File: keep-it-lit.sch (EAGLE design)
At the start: 33 parts, among them IC1 74AHCT1G04DBV, Q1 BSS138, Q2 BSS138, Q3 BSS138, Q4 BSS138

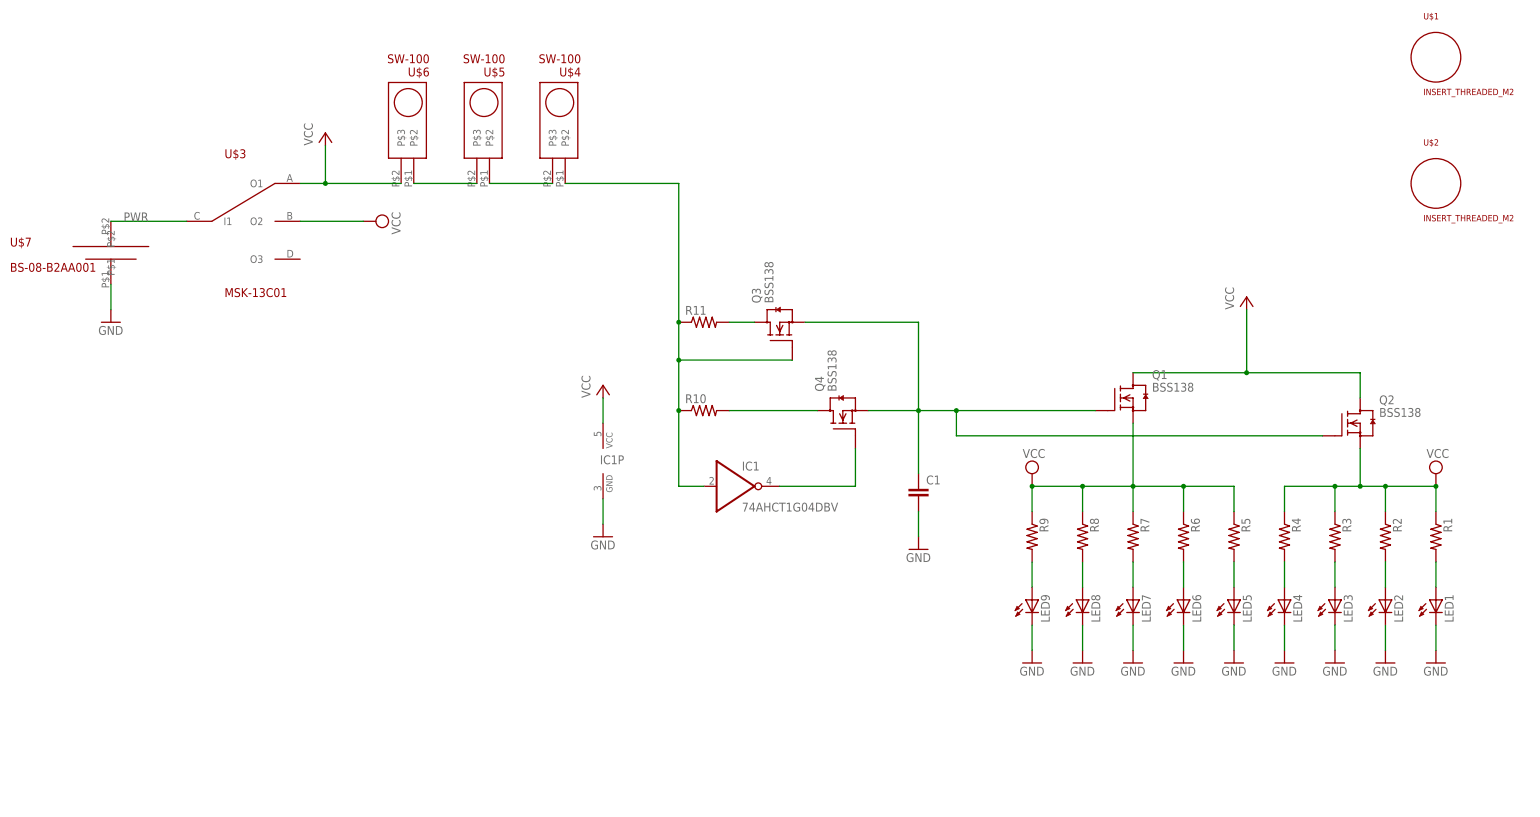
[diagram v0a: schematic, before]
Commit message: added lib, improved routing, fixed ground plane issues
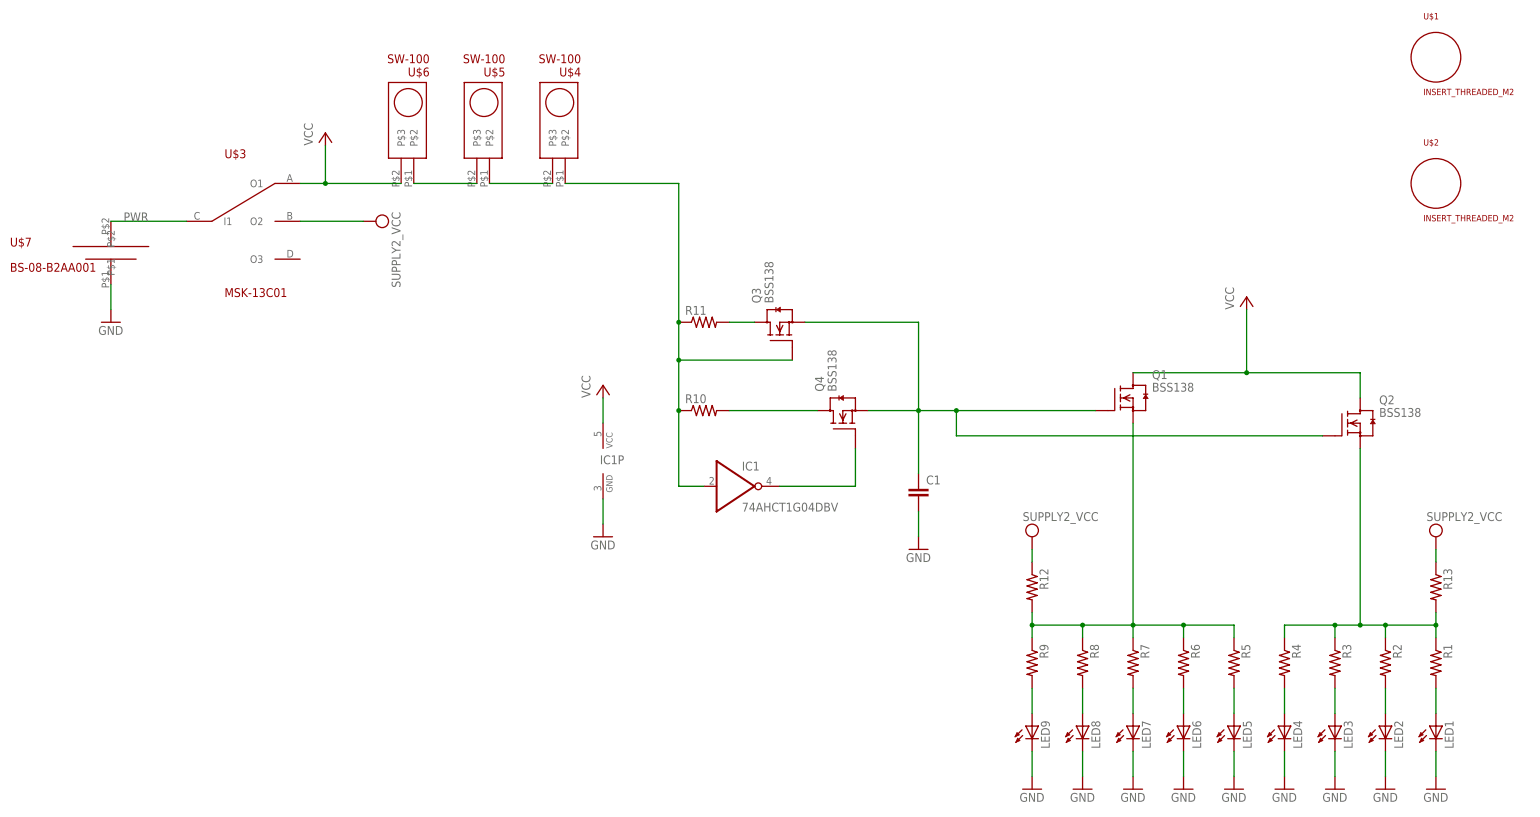
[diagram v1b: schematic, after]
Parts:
- added R12, R13: (no value), SparkFun-Passives:RESISTOR0603-RES
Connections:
- new net LED_GROUP1: Q1.S, R12.2, R5.1, R6.1, R7.1, R8.1, R9.1
- new net LED_GROUP2: Q2.S, R1.1, R13.2, R2.1, R3.1, R4.1
- new net VCC_ALLON: R12.1, R13.1, U$3.O2
- net VCC: no longer Q1.S, Q2.S, R1.1, R2.1, R3.1, R4.1, R5.1, R6.1, R7.1, R8.1, R9.1, U$3.O2
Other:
- moved on the sheet: LED1, LED2, LED3, LED4, LED5, LED6, LED7, LED8, LED9, R1, R2, R3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
